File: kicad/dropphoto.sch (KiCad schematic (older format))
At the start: 34 parts, among them J1 Conn_01x02, J2 Conn_01x02, J3 Conn_01x02, J4 Conn_01x02, J5 Conn_01x03, J6 Conn_01x03, J7 Conn_01x02, Q1 IRFZ44N, Q2 IRFZ44N, U1 Arduino_Nano_v3.x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

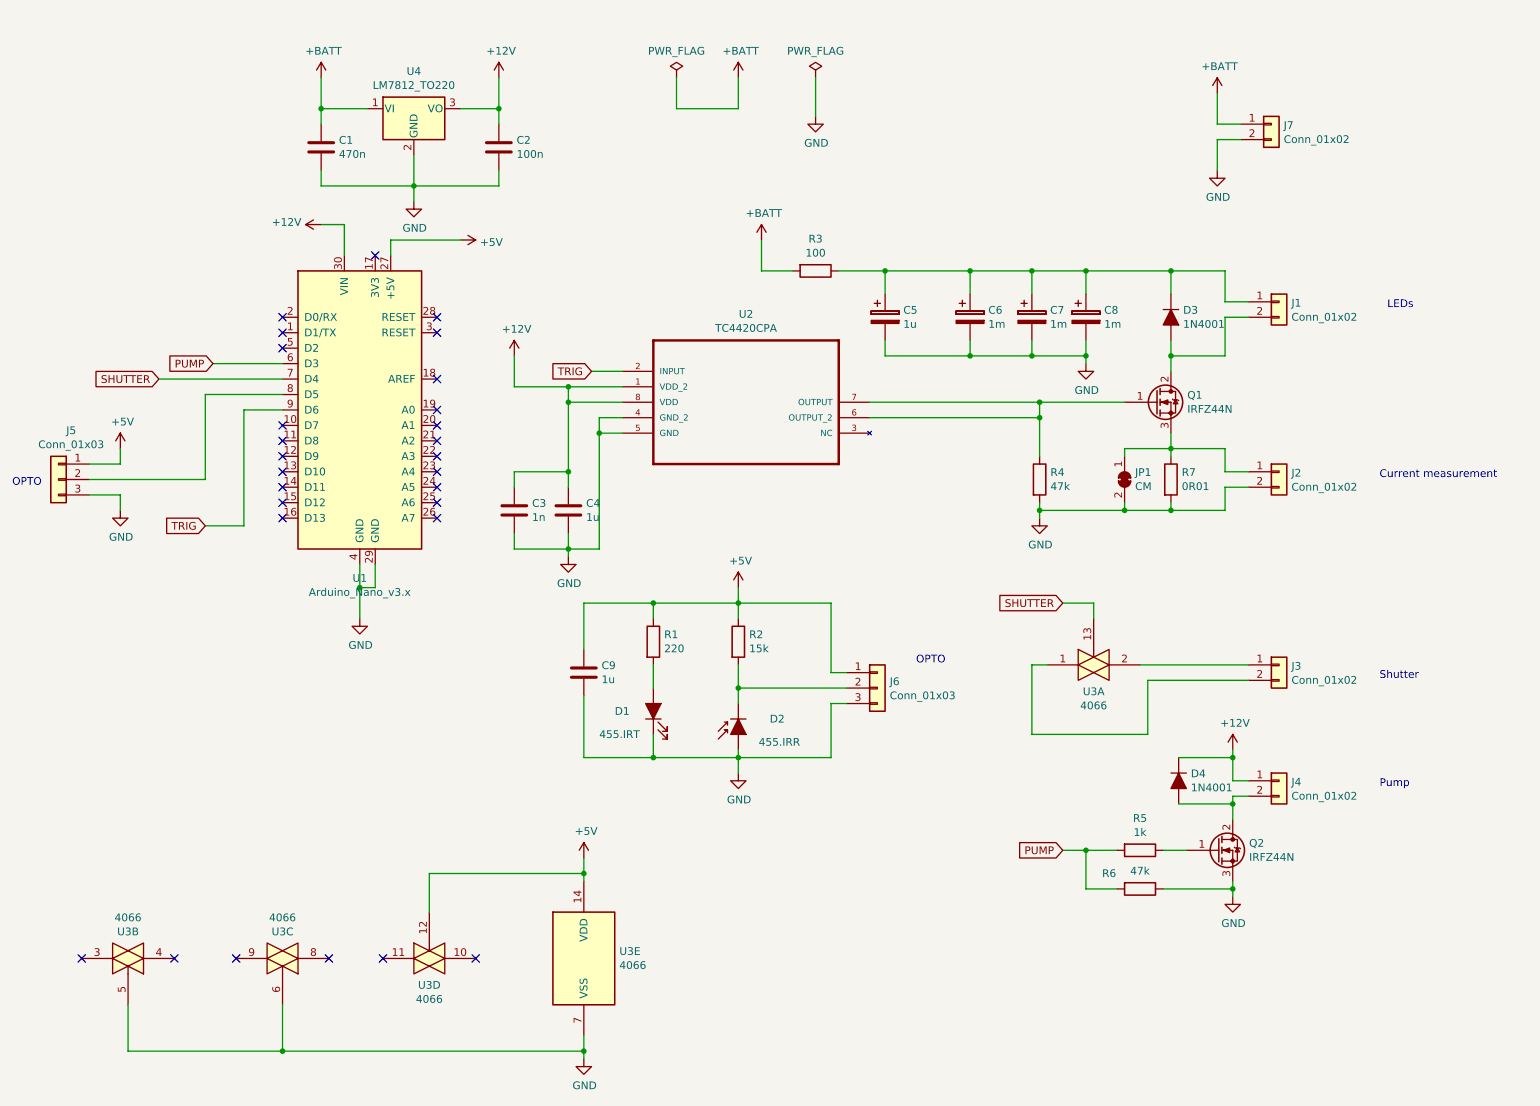
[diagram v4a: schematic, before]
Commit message: Finish routing.
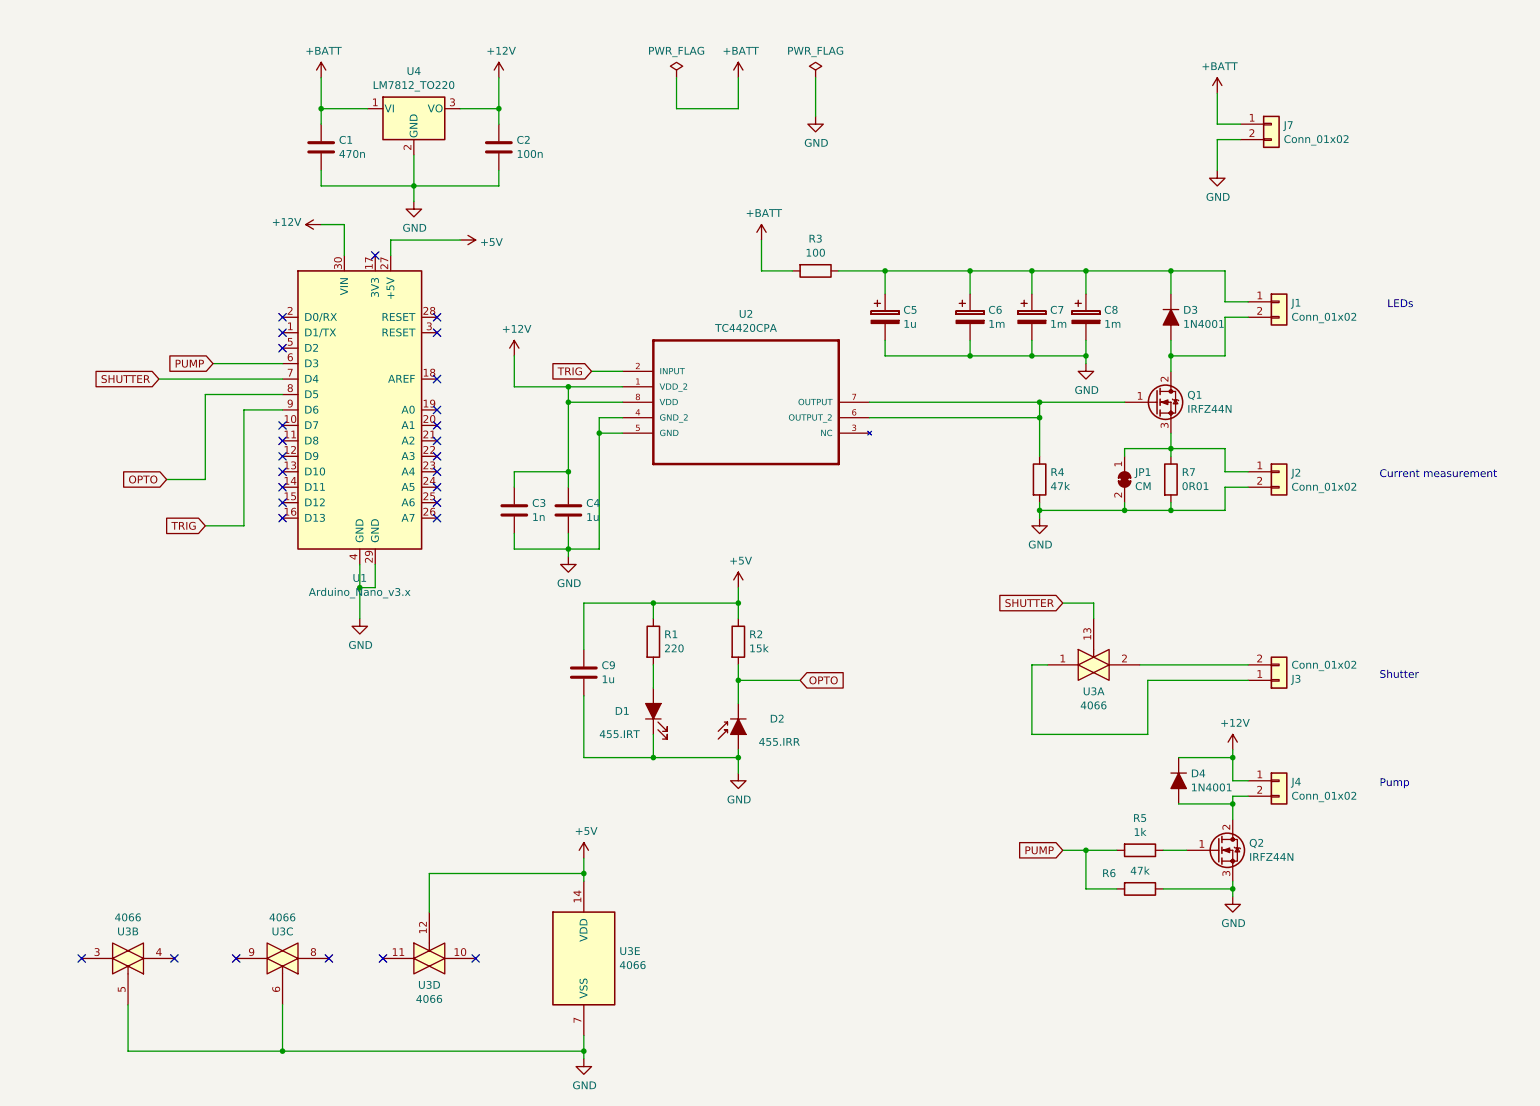
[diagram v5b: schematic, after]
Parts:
- removed J5, J6: Conn_01x03, Connector_JST:JST_XH_B03B-XH-A_1x03_P2.50mm_Vertical, symbol Connector_Generic:Conn_01x03
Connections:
- net OPTO: now reaches U1.8 (D5)
- net OPTO: now also D2.1 (K), R2.2
- net at U3.1: now also J3.1 (Pin_1); no longer J3.2 (Pin_2)
- net at U3.2: now also J3.2 (Pin_2); no longer J3.1 (Pin_1)
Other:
- note removed: "OPTO"
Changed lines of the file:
@@
 Wire Wire Line
 	8450 3500 8450 3550
-$Comp
-L Connector_Generic:Conn_01x02 J3
-U 1 1 5D006200
-P 9150 4900
-F 0 "J3" H 9230 4892 50  0000 L CNN
-F 1 "Conn_01x02" H 9230 4801 50  0000 L CNN
-F 2 "Connector_JST:JST_XH_B02B-XH-A_1x02_P2.50mm_Vertical" H 9150 4900 50  0001 C CNN
-F 3 "~" H 9150 4900 50  0001 C CNN
-	1    9150 4900
-	1    0    0    -1
-$EndComp
 Text Notes 9850 2600 0    50   ~ 0
 LEDs
@@
 Wire Wire Line
 	5650 4400 5650 4500
-Wire Wire Line
-	5650 4900 5650 5050
 $Comp
 L power:GND #PWR04
@@
 	1    0    0    -1
 $EndComp
-Wire Wire Line
-	5650 5050 6350 5050
-Connection ~ 5650 5050
-Wire Wire Line
-	5650 5050 5650 5150
 $Comp
 L MCU_Module:Arduino_Nano_v3.x U1
@@
 	5650 4500 5650 4600
 $Comp
-L Connector_Generic:Conn_01x03 J6
-U 1 1 5D16979A
-P 6550 5050
-F 0 "J6" H 6630 5092 50  0000 L CNN
-F 1 "Conn_01x03" H 6630 5001 50  0000 L CNN
-F 2 "Connector_JST:JST_XH_B03B-XH-A_1x03_P2.50mm_Vertical" H 6550 5050 50  0001 C CNN
-F 3 "~" H 6550 5050 50  0001 C CNN
-	1    6550 5050
-	1    0    0    -1
-$EndComp
-Wire Wire Line
-	6350 5150 6250 5150
-Wire Wire Line
-	6250 5150 6250 5500
-Wire Wire Line
-	6250 5500 5650 5500
-Wire Wire Line
-	6350 4950 6250 4950
-Wire Wire Line
-	6250 4950 6250 4500
-Wire Wire Line
-	6250 4500 5650 4500
-$Comp
 L Device:C C9
 U 1 1 5D176C99
@@
 	4650 5500 5100 5500
 Connection ~ 5100 5500
-$Comp
-L Connector_Generic:Conn_01x03 J5
-U 1 1 5D184B71
-P 1250 3700
-F 0 "J5" H 1168 4017 50  0000 C CNN
-F 1 "Conn_01x03" H 1168 3926 50  0000 C CNN
-F 2 "Connector_JST:JST_XH_B03B-XH-A_1x03_P2.50mm_Vertical" H 1250 3700 50  0001 C CNN
-F 3 "~" H 1250 3700 50  0001 C CNN
-	1    1250 3700
-	-1   0    0    -1
-$EndComp
-$Comp
-L power:+5V #PWR01
-U 1 1 5D193D6E
-P 1650 3500
-F 0 "#PWR01" H 1650 3350 50  0001 C CNN
-F 1 "+5V" H 1665 3673 50  0000 C CNN
-F 2 "" H 1650 3500 50  0001 C CNN
-F 3 "" H 1650 3500 50  0001 C CNN
-	1    1650 3500
-	1    0    0    -1
-$EndComp
-$Comp
-L power:GND #PWR02
-U 1 1 5D194213
-P 1650 3900
-F 0 "#PWR02" H 1650 3650 50  0001 C CNN
-F 1 "GND" H 1655 3727 50  0000 C CNN
-F 2 "" H 1650 3900 50  0001 C CNN
-F 3 "" H 1650 3900 50  0001 C CNN
-	1    1650 3900
-	1    0    0    -1
-$EndComp
-Wire Wire Line
-	1650 3900 1650 3800
-Wire Wire Line
-	1650 3800 1450 3800
-Wire Wire Line
-	1450 3600 1650 3600
-Wire Wire Line
-	1650 3600 1650 3500
 Wire Wire Line
 	2200 3150 2200 3700
-Wire Wire Line
-	2200 3700 1450 3700
-Text Notes 950  3750 0    50   ~ 0
-OPTO
-Text Notes 6800 4900 0    50   ~ 0
-OPTO
 $Comp
 L power:+12V #PWR0101
@@
 Wire Wire Line
 	6150 1350 6150 1100
+$Comp
+L Connector_Generic:Conn_01x02 J3
+U 1 1 5D006200
+P 9150 5000
+F 0 "J3" H 9230 4992 50  0000 L CNN
+F 1 "Conn_01x02" H 9230 4901 50  0000 L CNN
+F 2 "Connector_JST:JST_XH_B02B-XH-A_1x02_P2.50mm_Vertical" H 9150 5000 50  0001 C CNN
+F 3 "~" H 9150 5000 50  0001 C CNN
+	1    9150 5000
+	1    0    0    1
+$EndComp
+Text GLabel 1950 3700 0    50   Input ~ 0
+OPTO
+Wire Wire Line
+	1950 3700 2200 3700
+Wire Wire Line
+	5650 4900 5650 5000
+Text GLabel 6050 5000 2    50   Input ~ 0
+OPTO
+Wire Wire Line
+	6050 5000 5650 5000
+Connection ~ 5650 5000
+Wire Wire Line
+	5650 5000 5650 5150
 $EndSCHEMATC
